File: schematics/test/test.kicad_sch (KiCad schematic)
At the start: 33 parts, among them SW1 SW_Push, SW10 SW_Push, SW11 SW_Push, SW12 SW_Push, SW13 SW_DIP_x08, SW2 SW_Push, SW3 SW_Push, SW4 SW_Push, SW5 SW_Push, SW6 SW_Push, SW7 SW_Push, SW8 SW_Push, SW9 SW_Push

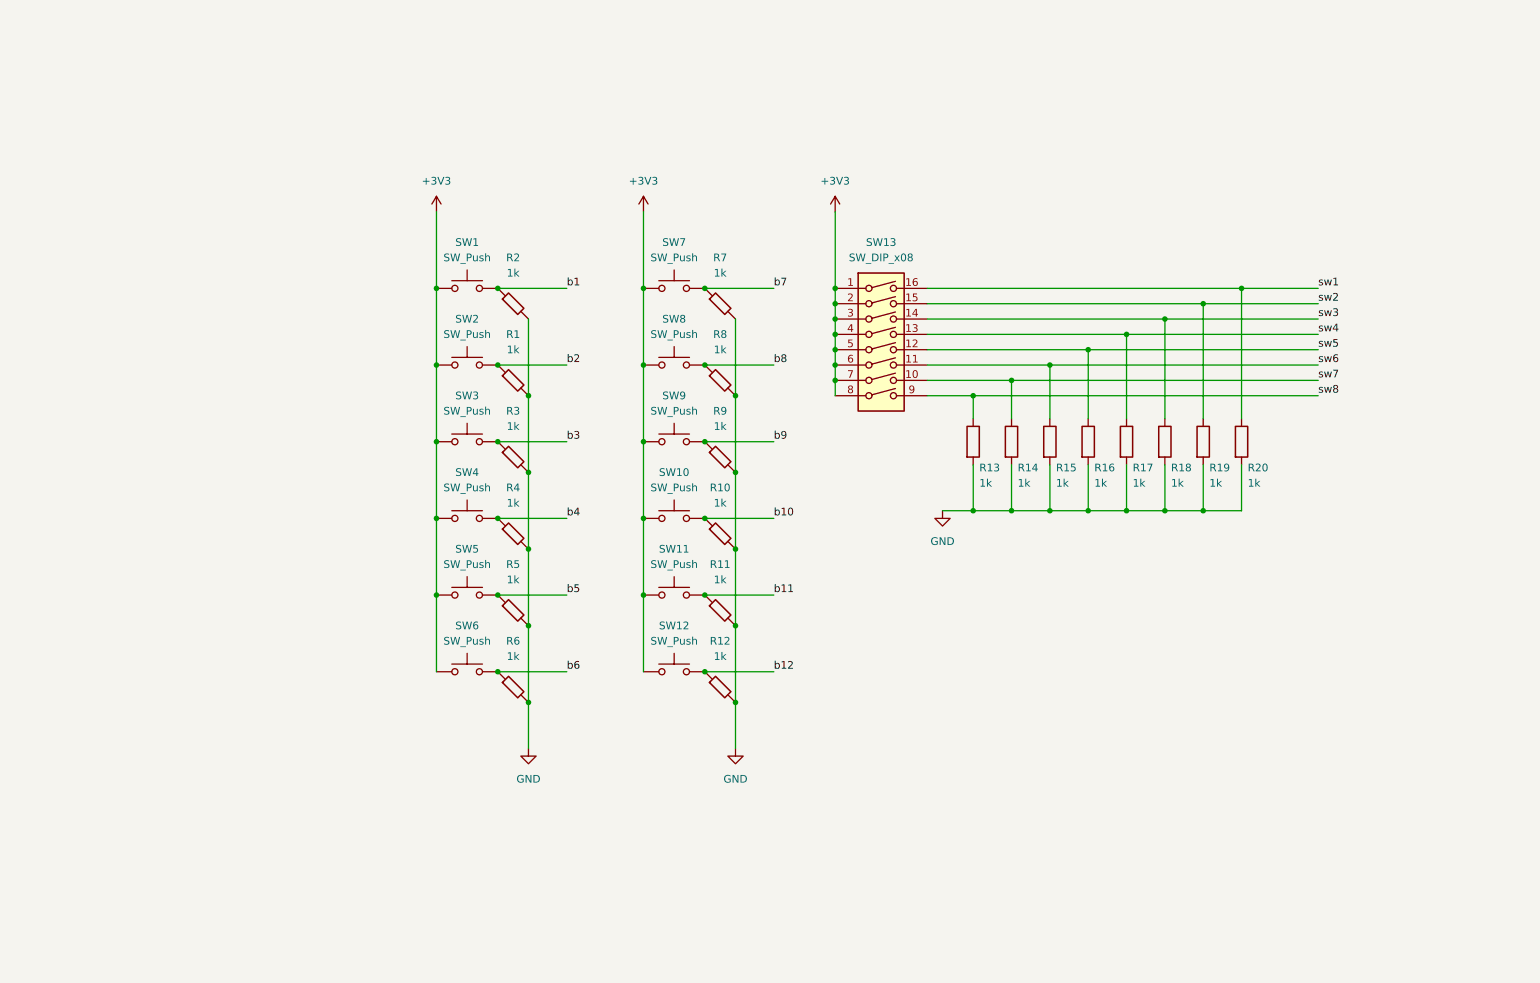
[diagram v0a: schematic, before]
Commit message: PUBLICATION.md update
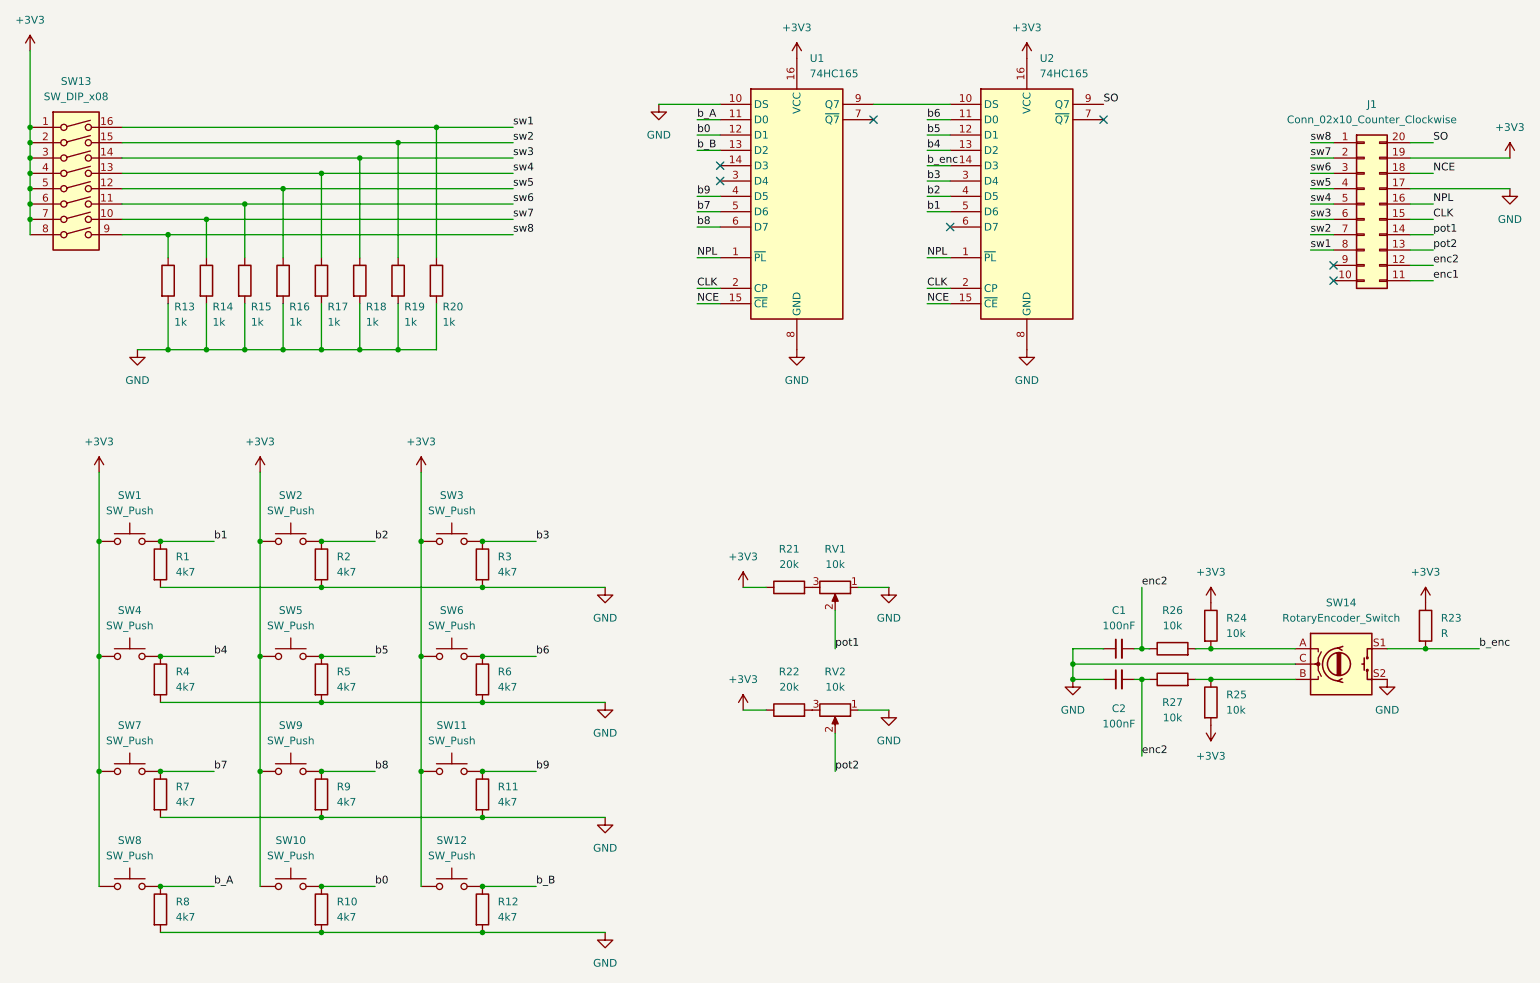
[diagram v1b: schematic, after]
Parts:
- removed R1, R10, R11, R12, R2, R3, R4, R5, R6, R7, R8, R9: 1k, symbol Device:R_45deg
- added C1, C2: 100nF, symbol Device:C_Small
- added J1: Conn_02x10_Counter_Clockwise, symbol Connector_Generic:Conn_02x10_Counter_Clockwise
- added R1, R10, R11, R12, R2, R3, R4, R5, R6, R7, R8, R9: 4k7, symbol Device:R
- added R21, R22: 20k, symbol Device:R
- added R23: R, symbol Device:R
- added R24, R25, R26, R27: 10k, symbol Device:R
- added RV1, RV2: 10k, symbol Device:R_Potentiometer
- added SW14: RotaryEncoder_Switch, symbol Device:RotaryEncoder_Switch
- added U1, U2: 74HC165, symbol 74xx:74HC165
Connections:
- net b11 is gone; now on net b9: SW11.2
- net +3V3: now also J1.19 (Pin_19), R21.1, R22.1, R23.1, R24.1, R25.2, U1.16 (VCC), U2.16 (VCC)
- net GND: now also C1.1, C2.1, J1.17 (Pin_17), R1.2, R10.2, R11.2, R12.2, R2.2, R3.2, R4.2, R5.2, R6.2, R7.2, R8.2, R9.2, RV1.1, RV2.1, SW14.C, SW14.S2, U1.10 (DS), U1.8 (GND), U2.8 (GND)
- net b1: now also R1.1, U2.5 (D6)
- net b2: now also R2.1, U2.4 (D5)
- net b3: now also R3.1, U2.3 (D4)
- net b4: now also R4.1, U2.13 (D2)
- net b5: now also R5.1, U2.12 (D1)
- net b6: now also R6.1, U2.11 (D0)
- net b7: now also R7.1, U1.5 (D6)
- net b8: now also SW9.2, R9.1, U1.6 (D7); no longer SW8.2
- net b9: now also R11.1, U1.4 (D5); no longer SW9.2
- net sw1: now also J1.8 (Pin_8)
- net sw2: now also J1.7 (Pin_7)
- net sw3: now also J1.6 (Pin_6)
- net sw4: now also J1.5 (Pin_5)
- net sw5: now also J1.4 (Pin_4)
- net sw6: now also J1.3 (Pin_3)
- net sw7: now also J1.2 (Pin_2)
- net sw8: now also J1.1 (Pin_1)
- net b10 renamed b0
- net b0: now also R10.1, U1.12 (D1)
- net b12 renamed b_B
- net b_B: now also R12.1, U1.13 (D2)
- new net: R25.1, R27.2, SW14.B
- new net: R24.2, R26.2, SW14.A
- new net: R21.2, RV1.3
- new net: R22.2, RV2.3
- new net: U1.9 (Q7), U2.10 (DS)
- new net CLK: J1.15 (Pin_15), U1.2 (CP), U2.2 (CP)
- new net NCE: J1.18 (Pin_18), U1.15 (~{CE}), U2.15 (~{CE})
- new net NPL: J1.16 (Pin_16), U1.1 (~{PL}), U2.1 (~{PL})
- new net SO: J1.20 (Pin_20), U2.9 (Q7)
- new net b_A: R8.1, SW8.2, U1.11 (D0)
- new net b_enc: R23.2, SW14.S1, U2.14 (D3)
- new net enc1: J1.11 (Pin_11)
- new net enc2: C1.2, C2.2, J1.12 (Pin_12), R26.1, R27.1
- new net pot1: J1.14 (Pin_14), RV1.2
- new net pot2: J1.13 (Pin_13), RV2.2
- no-connect marks 0 -> 7
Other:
- moved on the sheet: R13, R14, R15, R16, R17, R18, R19, R20, SW13

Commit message: a lot of stuff
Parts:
- removed C1, C2: 100nF, symbol Device:C_Small
- removed J1: Conn_02x10_Counter_Clockwise, symbol Connector_Generic:Conn_02x10_Counter_Clockwise
- removed R13, R14, R15, R16, R17, R18, R19, R20: 1k, symbol Device:R
- removed R21, R22: 20k, symbol Device:R
- removed R23: R, symbol Device:R
- removed R24, R25, R26, R27: 10k, symbol Device:R
- removed RV1, RV2: 10k, symbol Device:R_Potentiometer
- removed SW13: SW_DIP_x08, symbol Switch:SW_DIP_x08
- removed SW14: RotaryEncoder_Switch, symbol Device:RotaryEncoder_Switch
- added MIK32: (no value), symbol cunstom:MIK32_SPI
- added R28: 10 кОм, symbol Device:R
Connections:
- net NCE is gone; now on net GND: U1.15 (~{CE}), U2.15 (~{CE})
- net +3V3: now also MIK32. (GND)
- net CLK: now also MIK32. (GND)
- net GND: now also MIK32. (GND)
- net NPL: now also MIK32. (GND)
- net SO: no longer names the net of U2.9 (Q7)
- net SO: now also R28.1
- new net: MIK32. (GND), R28.2
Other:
- moved on the sheet: R1, R10, R11, R12, R2, R3, R4, R5, R6, R7, R8, R9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
